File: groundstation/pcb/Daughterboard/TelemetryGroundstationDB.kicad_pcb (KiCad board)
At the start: 2 copper layers, 90 x 90 mm, 32 parts, among them J1 RFPC-SMA27-F, J2 ICD15S13E4GV00LF, M1 M4 Mounting Hole, M2 M4 Mounting Hole, M3 M4 Mounting Hole, M4 M4 Mounting Hole, U1 RC1780HP-RC232

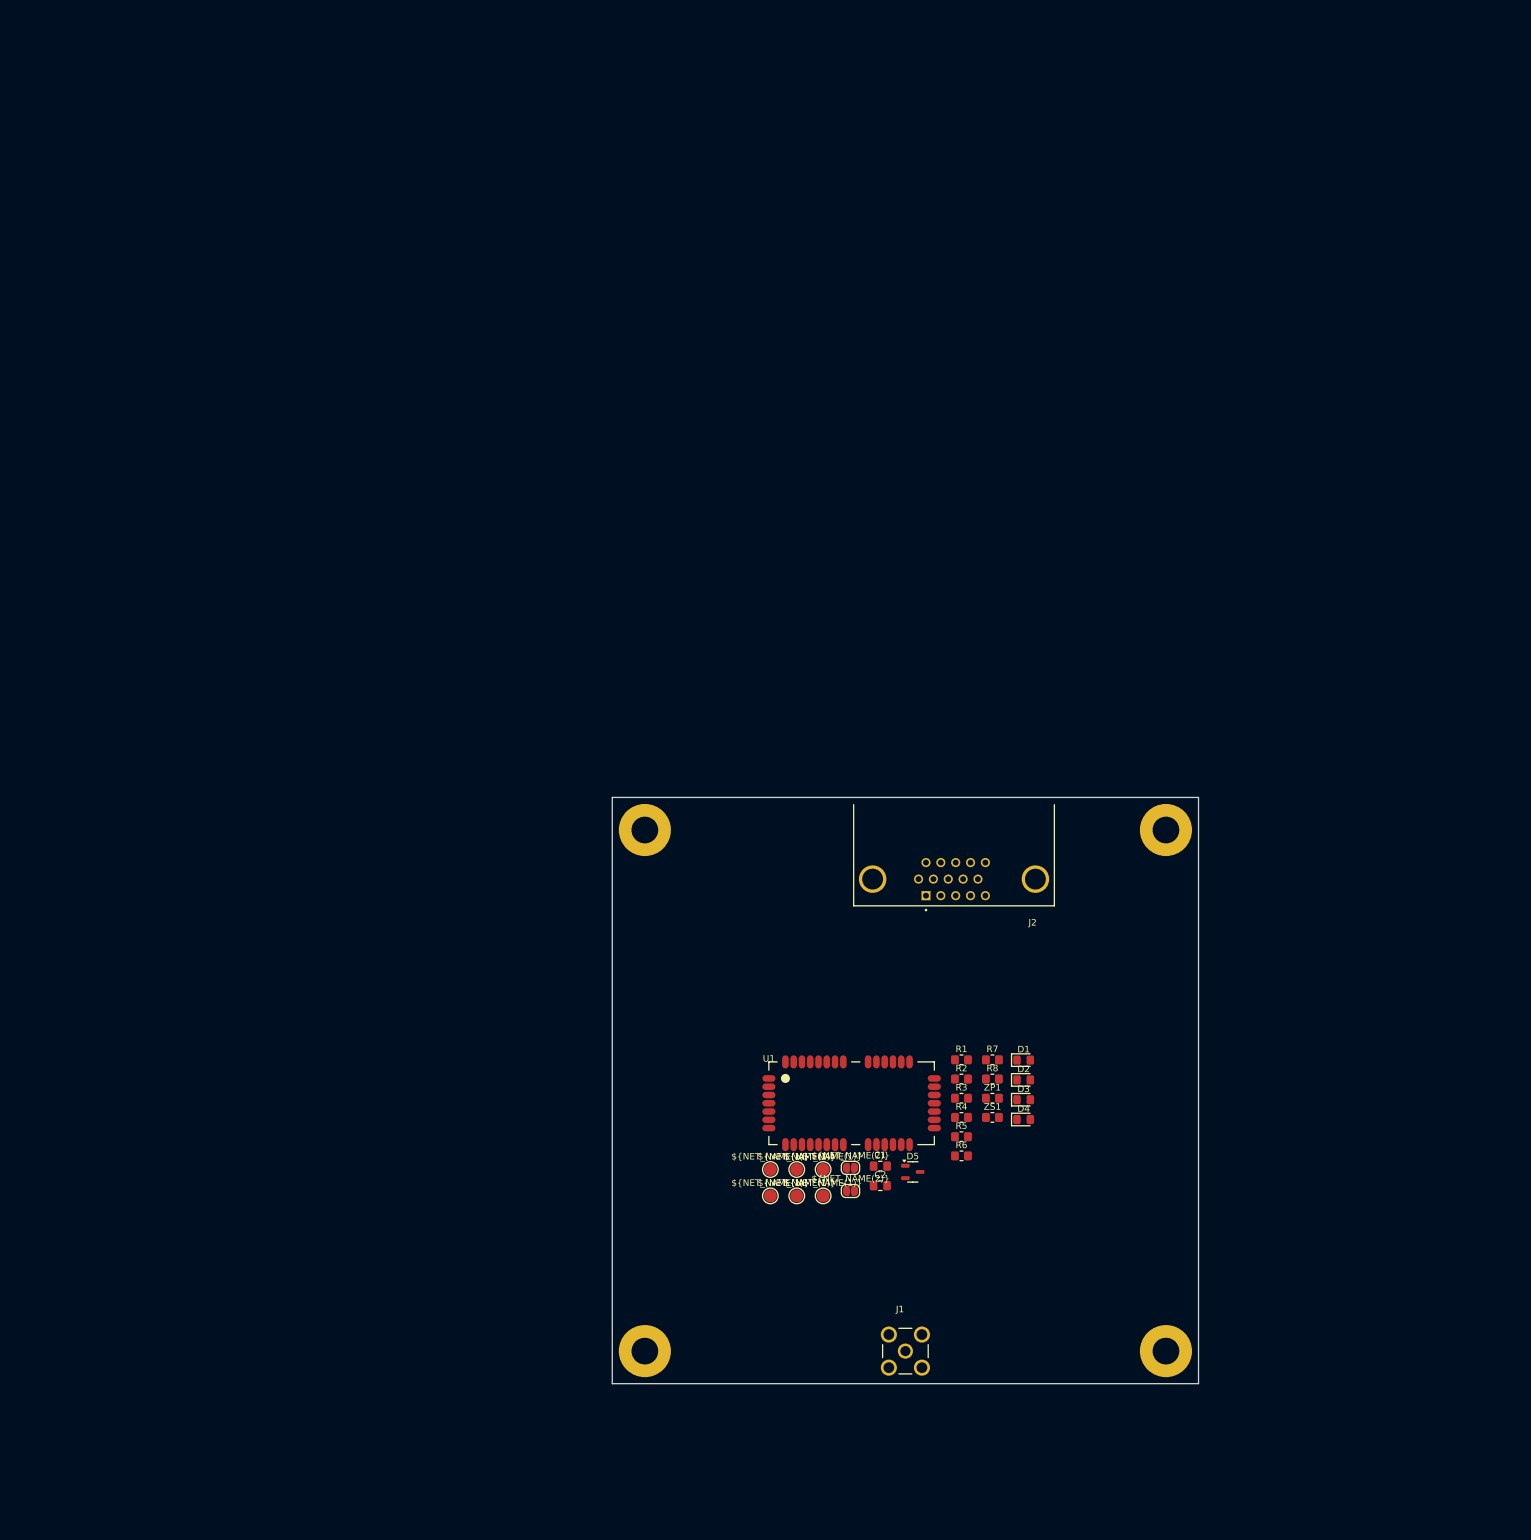
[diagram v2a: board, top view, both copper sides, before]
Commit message: change hd15 pin positions
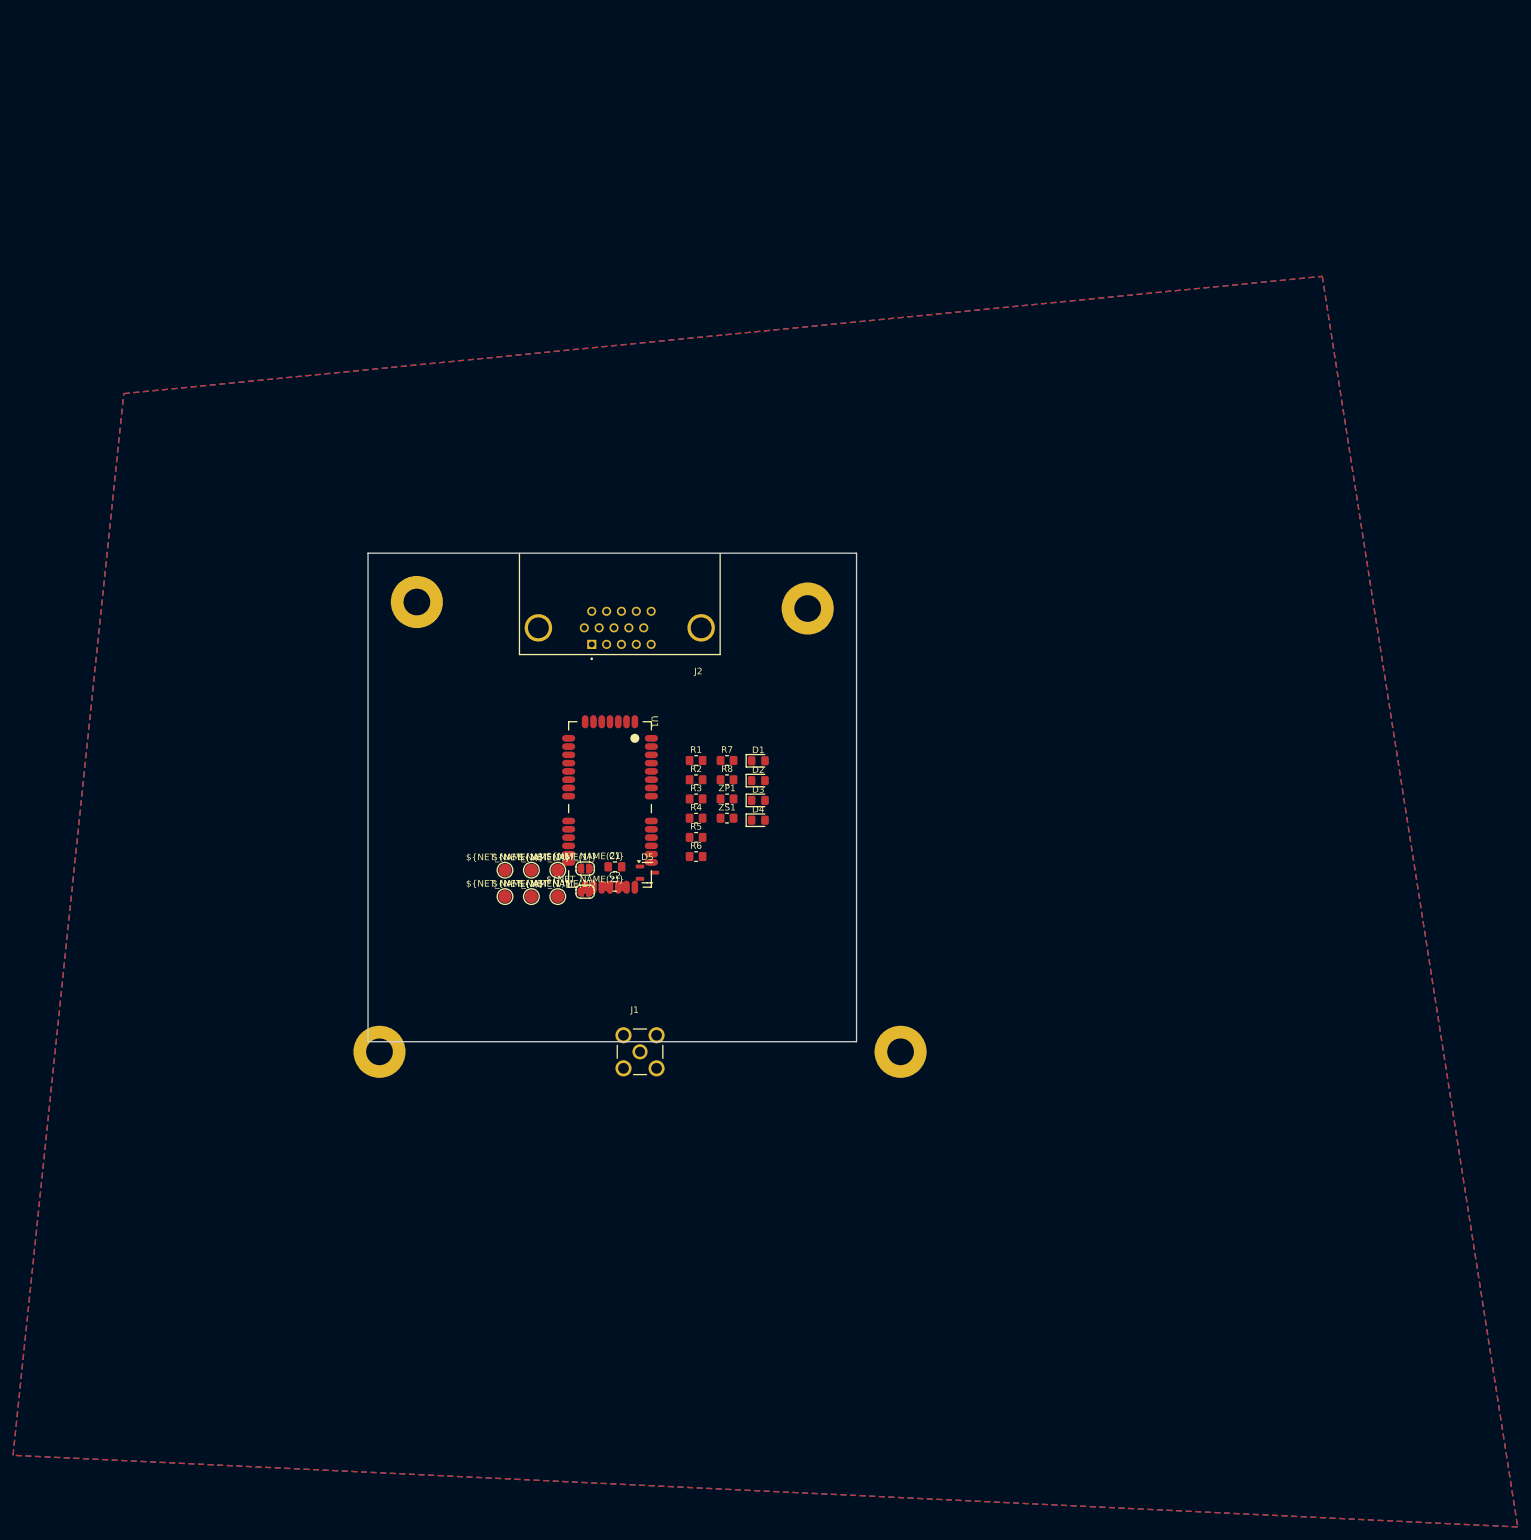
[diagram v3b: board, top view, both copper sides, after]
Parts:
- moved M2 64.7 mm to (30.0, -29.0)
- moved J2 64.2 mm to (1.15, -26.0)
- moved C1 61.4 mm to (0.41, 10.7)
- moved C2 61.4 mm to (0.41, 13.7)
- moved D1 61.4 mm to (22.4, -5.62)
- moved D2 61.4 mm to (22.4, -2.58)
- moved D3 61.4 mm to (22.4, 0.46)
- moved D4 61.4 mm to (22.4, 3.50)
- moved J1 61.4 mm to (4.26, 39.0)
- moved JP2 61.4 mm to (-4.16, 14.5)
- moved M1 61.4 mm to (44.3, 39.0)
- moved M4 61.4 mm to (-35.7, 39.0)
- moved R1 61.4 mm to (12.9, -5.67)
- moved R3 61.4 mm to (12.9, 0.23)
- moved R4 61.4 mm to (12.9, 3.18)
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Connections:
- J2 pad 1: RTS -> TX
- J2 pad 10: +5V -> +3V3
- J2 pad 11: +3V3 -> GND
- J2 pad 13: +5V -> GND
- J2 pad 14: GND -> +5V
- J2 pad 2: CTS -> RX
- J2 pad 4: RST -> RTS
- J2 pad 5: +3V3 -> CTS
- J2 pad 6: TX -> RST
- J2 pad 7: RX -> GND
- J2 pad 8: +3V3 -> GND
- J2 pad 9: GND -> +3V3
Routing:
- added copper zone on B.Cu, net GND
- added copper zone on F.Cu, net GND
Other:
- board size 90 x 90 mm -> 75 x 75 mm

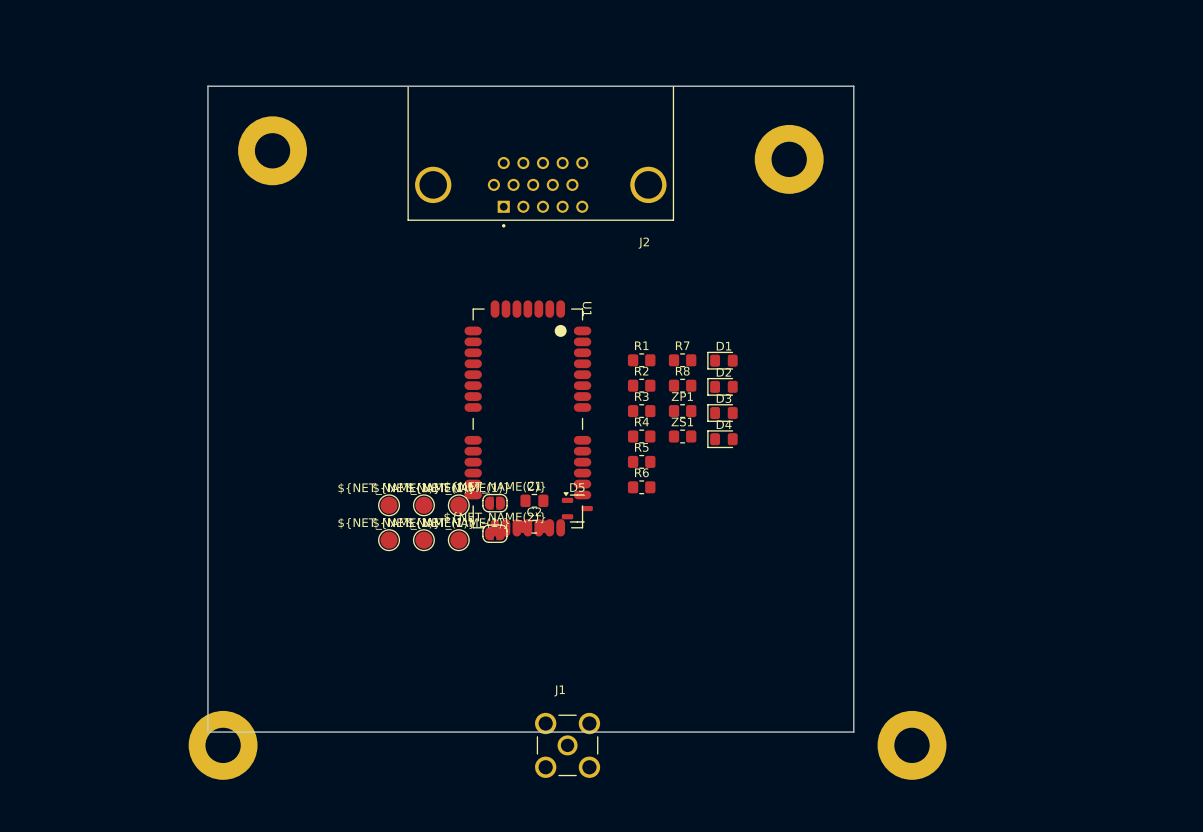
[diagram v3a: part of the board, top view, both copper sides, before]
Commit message: started daughterboard pcb design
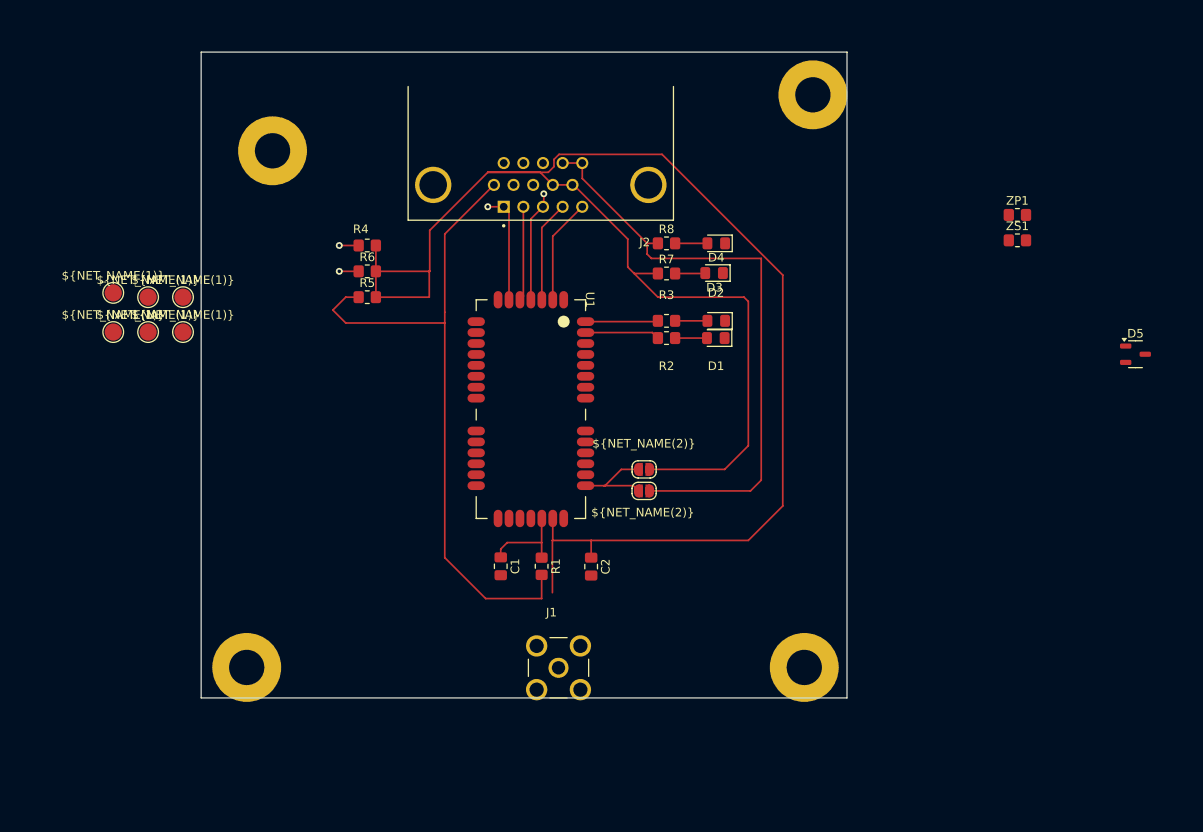
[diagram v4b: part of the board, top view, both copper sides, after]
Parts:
- moved D5 67.3 mm to (70.2, -6.38)
- moved ZP1 45.1 mm to (56.5, -22.6)
- moved ZS1 45.1 mm to (56.5, -19.6)
- moved R6 40.6 mm to (-19.0, -16.0)
- moved TP1 40.4 mm to (-48.5, -13.5)
- moved TP2 40.1 mm to (-48.5, -8.95)
- moved TP3 40.1 mm to (-44.5, -13.0)
- moved TP4 40.1 mm to (-44.5, -8.95)
- moved TP5 40.1 mm to (-40.4, -13.0)
- moved TP6 40.1 mm to (-40.4, -8.95)
- moved R4 38.8 mm to (-19.0, -19.0)
- moved R5 37.2 mm to (-19.0, -13.0)
- moved R1 26.6 mm to (1.25, 18.2), turned to -90 degrees
- moved D4 22.8 mm to (21.5, -19.2), turned to 180 degrees
- moved JP2 18.8 mm to (13.1, 7.00), turned to 180 degrees
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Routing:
- net +3V3: track 0.00 -> 213.5 mm
- net RST: track 0.00 -> 78.9 mm
- net +5V: track 0.00 -> 69.9 mm
- net CFG: track 0.00 -> 15.2 mm, vias 0 -> 2
- net TX: track 0.00 -> 15.1 mm, vias 0 -> 2
- net CTS: track 0.00 -> 12.2 mm
- net RTS: track 0.00 -> 11.8 mm
- net Net-(JP1-B): track 0.00 -> 11.2 mm
- net RX: track 0.00 -> 11.0 mm
- net Net-(U1-RESET): track 0.00 -> 10.6 mm
- net Net-(U1-D1): track 0.00 -> 8.67 mm
- net Net-(U1-D2): track 0.00 -> 8.44 mm
- net Net-(D4-A): track 0.00 -> 3.75 mm
- net Net-(D2-A): track 0.00 -> 3.75 mm
- net Net-(D1-A): track 0.00 -> 3.70 mm
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
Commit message: Daughterboard PCB design worked on
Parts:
- moved ZP1 94.8 mm to (-27.5, 21.5), turned to 180 degrees
- moved ZS1 91.3 mm to (-26.5, 18.5), turned to -90 degrees
- moved D5 79.5 mm to (-3.82, -35.3)
- moved R5 38.0 mm to (-15.0, 24.8), turned to 90 degrees
- moved JP1 35.3 mm to (4.04, -24.6), turned to -90 degrees
- moved JP2 32.3 mm to (6.54, -24.6), turned to -90 degrees
- moved TP4 31.3 mm to (-15.8, -21.5)
- moved J1 29.9 mm to (-26.5, 27.0)
- moved C2 27.4 mm to (-20.4, 17.5), turned to 0 degrees
- moved J2 27.3 mm to (-24.0, -36.8)
- moved TP2 26.9 mm to (-24.8, -21.5)
- moved D3 25.9 mm to (-3.91, -21.7), turned to 90 degrees
- moved M3 25.2 mm to (-54.2, -36.8)
- moved TP6 25.0 mm to (-18.8, -21.5)
- moved U1 24.1 mm to (-17.6, -10.4)
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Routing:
- net +3V3: track 213.5 -> 110.3 mm
- net RST: track 78.9 -> 146.5 mm
- net Net-(JP1-B): track 11.2 -> 55.3 mm
- net +5V: track 69.9 -> 48.0 mm
- net CTS: track 12.2 -> 28.1 mm
- net RTS: track 11.8 -> 26.5 mm
- net RX: track 11.0 -> 24.1 mm
- net CFG: track 15.2 -> 26.0 mm, vias 2 -> 0
- net TX: track 15.1 -> 25.5 mm, vias 2 -> 0
- net Net-(J1-Pad1): track 0.00 -> 7.50 mm
- net Net-(U1-RF): track 0.00 -> 2.56 mm
- net Net-(U1-D1): track 8.67 -> 9.42 mm
- net Net-(U1-RESET): track 10.6 -> 9.93 mm
- net GND: vias 0 -> 14
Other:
- board size 75 x 75 mm -> 100 x 75 mm
